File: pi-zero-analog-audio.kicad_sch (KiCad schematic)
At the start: 33 parts, among them J1 GPIO, J2 Screw_Terminal_01x04, J3 Audio Jack, U1 MIC5365-3.3YD5, U2 MC74VHC1GT50, U3 MC74VHC1GT50, U4 PAM8403D

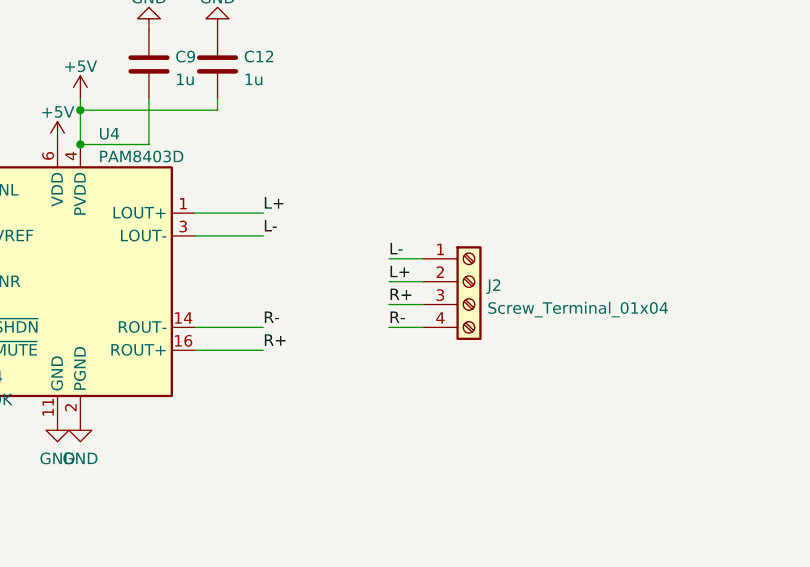
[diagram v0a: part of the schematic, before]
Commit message: Wiring the amplifier on the right side
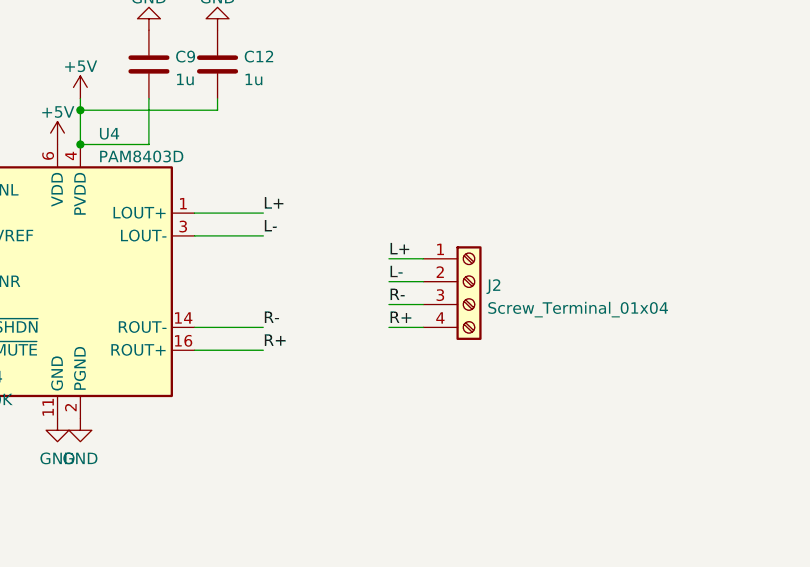
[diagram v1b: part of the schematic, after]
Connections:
- net L+: now also J2.1 (Pin_1); no longer J2.2 (Pin_2)
- net L-: now also J2.2 (Pin_2); no longer J2.1 (Pin_1)
- net R+: now also J2.4 (Pin_4); no longer J2.3 (Pin_3)
- net R-: now also J2.3 (Pin_3); no longer J2.4 (Pin_4)

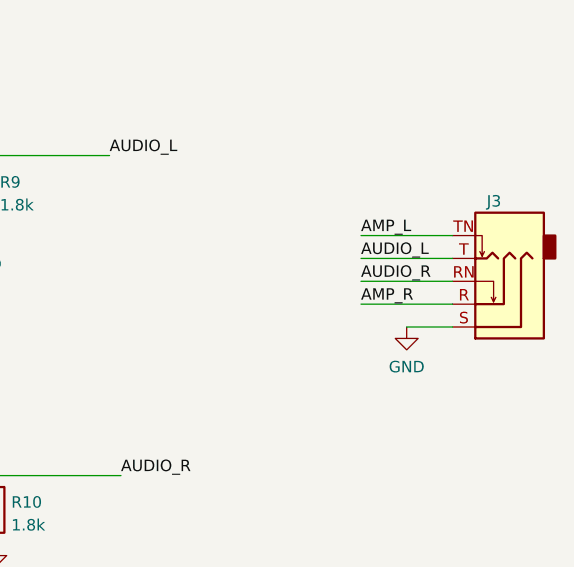
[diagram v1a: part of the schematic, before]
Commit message: Some more efficient design with the same components
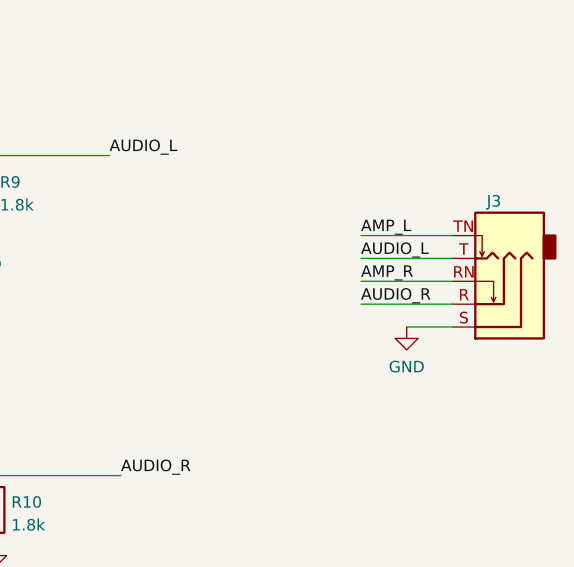
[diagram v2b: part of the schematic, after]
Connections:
- net AMP_R: now also J3.RN; no longer J3.R
- net AUDIO_R: now also J3.R; no longer J3.RN
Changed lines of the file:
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@@
     (stroke (width 0) (type default) (color 0 0 0 0))
+  )
+  (wire (pts (xy 40.64 64.77) (xy 38.1 64.77))
+    (stroke (width 0) (type solid) (color 0 0 0 0))
+  )
+  (wire (pts (xy 162.56 127) (xy 166.37 127))
+    (stroke (width 0) (type default) (color 0 0 0 0))
+  )
+  (wire (pts (xy 76.2 137.16) (xy 85.09 137.16))
+    (stroke (width 0) (type default) (color 0 0 0 0))
+  )
+  (wire (pts (xy 104.14 139.7) (xy 104.14 134.62))
+    (stroke (width 0) (type default) (color 0 0 0 0))
+  )
+  (wire (pts (xy 120.65 33.02) (xy 120.65 22.86))
+    (stroke (width 0) (type default) (color 0 0 0 0))
+  )
+  (wire (pts (xy 146.05 30.48) (xy 152.4 30.48))
+    (stroke (width 0) (type default) (color 0 0 0 0))
+  )
+  (wire (pts (xy 109.22 19.05) (xy 109.22 22.86))
+    (stroke (width 0) (type default) (color 0 0 0 0))
+  )
+  (wire (pts (xy 160.02 30.48) (xy 173.99 30.48))
+    (stroke (width 0) (type default) (color 0 0 0 0))
+  )
+  (wire (pts (xy 40.64 24.13) (xy 40.64 26.67))
+    (stroke (width 0) (type solid) (color 0 0 0 0))
+  )
+  (wire (pts (xy 38.1 62.23) (xy 43.18 62.23))
+    (stroke (width 0) (type default) (color 0 0 0 0))
+  )
+  (wire (pts (xy 201.93 44.45) (xy 212.09 44.45))
+    (stroke (width 0) (type default) (color 0 0 0 0))
+  )
+  (wire (pts (xy 62.23 30.48) (xy 62.23 35.56))
+    (stroke (width 0) (type default) (color 0 0 0 0))
+  )
+  (wire (pts (xy 40.64 39.37) (xy 40.64 46.99))
+    (stroke (width 0) (type solid) (color 0 0 0 0))
+  )
+  (wire (pts (xy 40.64 39.37) (xy 38.1 39.37))
+    (stroke (width 0) (type solid) (color 0 0 0 0))
+  )
+  (wire (pts (xy 104.14 147.32) (xy 104.14 146.05))
+    (stroke (width 0) (type default) (color 0 0 0 0))
+  )
+  (wire (pts (xy 40.64 20.32) (xy 40.64 24.13))
+    (stroke (width 0) (type solid) (color 0 0 0 0))
+  )
+  (wire (pts (xy 140.97 134.62) (xy 148.59 134.62))
+    (stroke (width 0) (type default) (color 0 0 0 0))
+  )
+  (wire (pts (xy 40.64 24.13) (xy 38.1 24.13))
+    (stroke (width 0) (type solid) (color 0 0 0 0))
   )
   (wire (pts (xy 201.93 41.91) (xy 212.09 41.91))
     (stroke (width 0) (type default) (color 0 0 0 0))
   )
-  (wire (pts (xy 40.64 64.77) (xy 38.1 64.77))
-    (stroke (width 0) (type solid) (color 0 0 0 0))
-  )
-  (wire (pts (xy 162.56 127) (xy 166.37 127))
-    (stroke (width 0) (type default) (color 0 0 0 0))
-  )
-  (wire (pts (xy 76.2 137.16) (xy 85.09 137.16))
-    (stroke (width 0) (type default) (color 0 0 0 0))
-  )
-  (wire (pts (xy 104.14 139.7) (xy 104.14 134.62))
-    (stroke (width 0) (type default) (color 0 0 0 0))
-  )
-  (wire (pts (xy 120.65 33.02) (xy 120.65 22.86))
-    (stroke (width 0) (type default) (color 0 0 0 0))
-  )
-  (wire (pts (xy 146.05 30.48) (xy 152.4 30.48))
-    (stroke (width 0) (type default) (color 0 0 0 0))
-  )
-  (wire (pts (xy 109.22 19.05) (xy 109.22 22.86))
-    (stroke (width 0) (type default) (color 0 0 0 0))
-  )
-  (wire (pts (xy 160.02 30.48) (xy 173.99 30.48))
-    (stroke (width 0) (type default) (color 0 0 0 0))
-  )
-  (wire (pts (xy 40.64 24.13) (xy 40.64 26.67))
-    (stroke (width 0) (type solid) (color 0 0 0 0))
-  )
-  (wire (pts (xy 38.1 62.23) (xy 43.18 62.23))
-    (stroke (width 0) (type default) (color 0 0 0 0))
-  )
-  (wire (pts (xy 201.93 44.45) (xy 212.09 44.45))
-    (stroke (width 0) (type default) (color 0 0 0 0))
-  )
-  (wire (pts (xy 62.23 30.48) (xy 62.23 35.56))
-    (stroke (width 0) (type default) (color 0 0 0 0))
-  )
-  (wire (pts (xy 40.64 39.37) (xy 40.64 46.99))
-    (stroke (width 0) (type solid) (color 0 0 0 0))
-  )
-  (wire (pts (xy 40.64 39.37) (xy 38.1 39.37))
-    (stroke (width 0) (type solid) (color 0 0 0 0))
-  )
-  (wire (pts (xy 104.14 147.32) (xy 104.14 146.05))
-    (stroke (width 0) (type default) (color 0 0 0 0))
-  )
-  (wire (pts (xy 40.64 20.32) (xy 40.64 24.13))
-    (stroke (width 0) (type solid) (color 0 0 0 0))
-  )
-  (wire (pts (xy 140.97 134.62) (xy 148.59 134.62))
-    (stroke (width 0) (type default) (color 0 0 0 0))
-  )
-  (wire (pts (xy 40.64 24.13) (xy 38.1 24.13))
-    (stroke (width 0) (type solid) (color 0 0 0 0))
-  )
   (wire (pts (xy 120.65 22.86) (xy 109.22 22.86))
     (stroke (width 0) (type default) (color 0 0 0 0))
@@
     (effects (font (size 1.27 1.27)) (justify left bottom))
   )
-  (label "AUDIO_R" (at 201.93 44.45 0)
-    (effects (font (size 1.27 1.27)) (justify left bottom))
-  )
   (label "AMP_L" (at 76.2 119.38 0)
     (effects (font (size 1.27 1.27)) (justify left bottom))
   )
+  (label "AUDIO_R" (at 201.93 46.99 0)
+    (effects (font (size 1.27 1.27)) (justify left bottom))
+  )
   (label "MUTE" (at 76.2 137.16 0)
     (effects (font (size 1.27 1.27)) (justify left bottom))
@@
     (effects (font (size 1.27 1.27)) (justify left bottom))
   )
-  (label "AMP_R" (at 201.93 46.99 0)
-    (effects (font (size 1.27 1.27)) (justify left bottom))
-  )
   (label "MUTE" (at 43.18 67.31 0)
     (effects (font (size 1.27 1.27)) (justify left bottom))
@@
     (effects (font (size 1.27 1.27)) (justify left bottom))
   )
+  (label "AMP_R" (at 201.93 44.45 0)
+    (effects (font (size 1.27 1.27)) (justify left bottom))
+  )

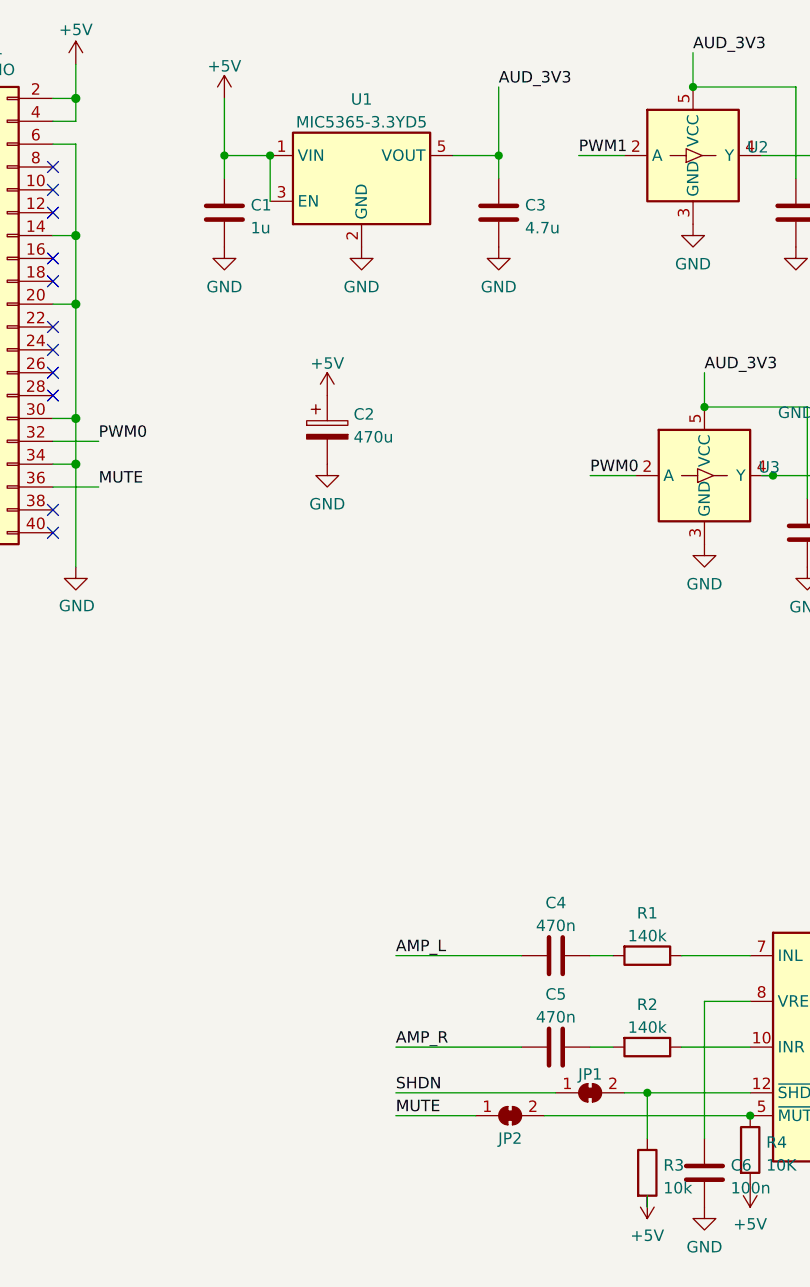
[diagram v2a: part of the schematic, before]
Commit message: Allow alternate LDO with Band-Gap Bypass
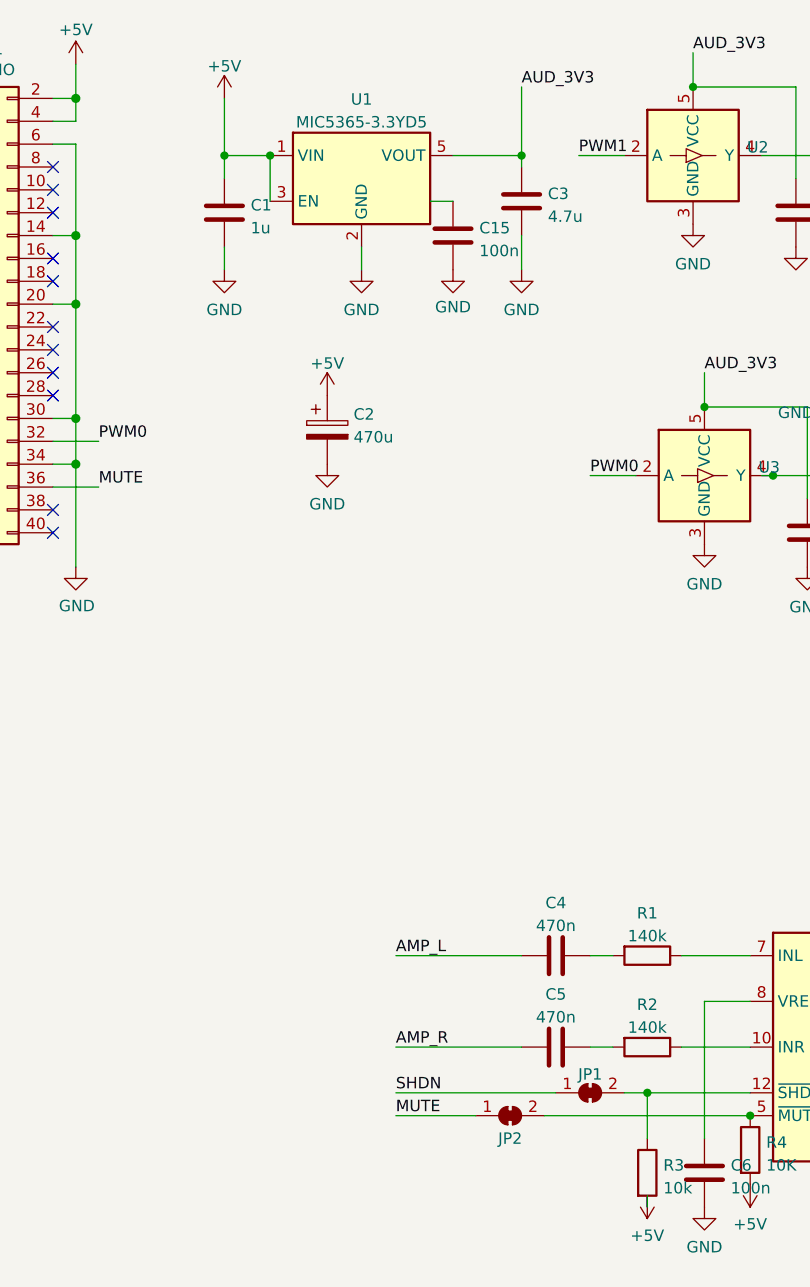
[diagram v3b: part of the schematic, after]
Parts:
- added C15: 100n, Capacitor_SMD:C_0805_2012Metric_Pad1.18x1.45mm_HandSolder, symbol Device:C
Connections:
- net GND: now also C15.2
- net at U1.4 (NC): now also C15.1
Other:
- moved on the sheet: C3

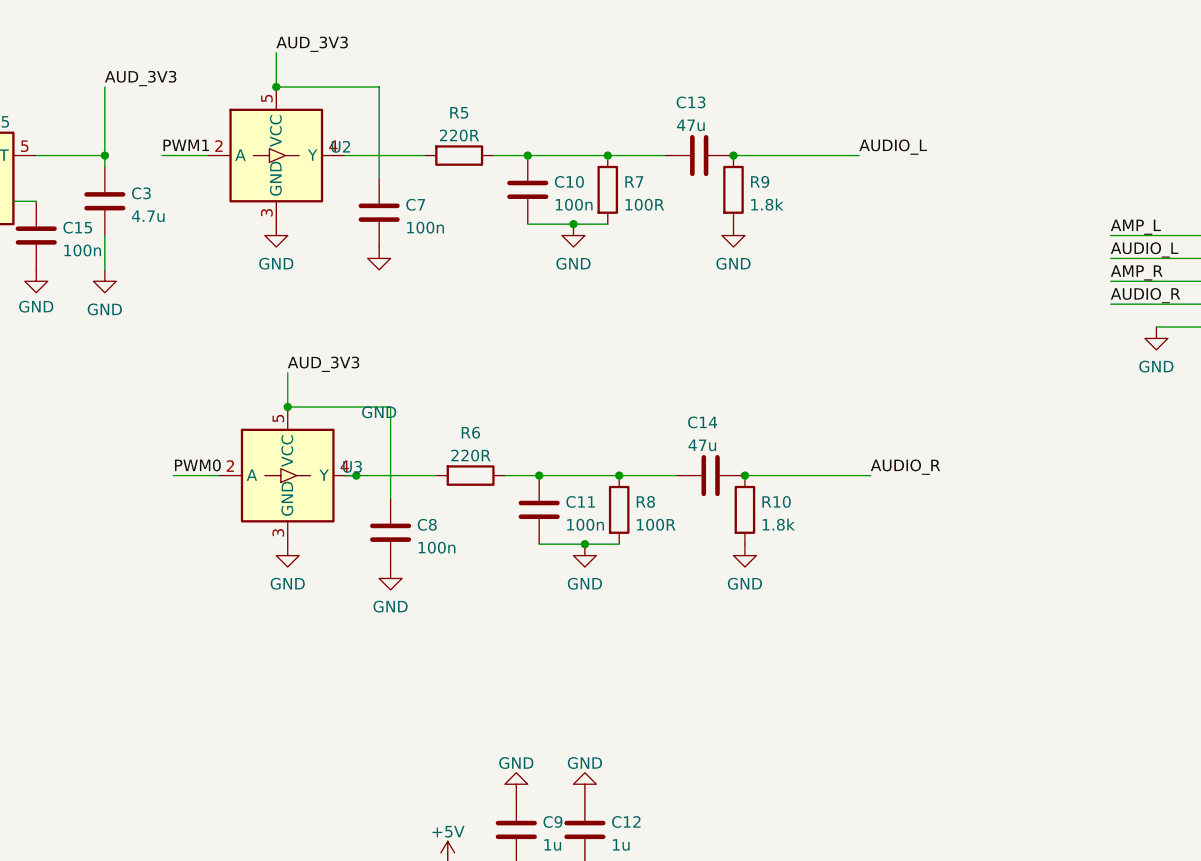
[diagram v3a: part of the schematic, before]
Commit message: Adding ferrite beads on 3V3 rails
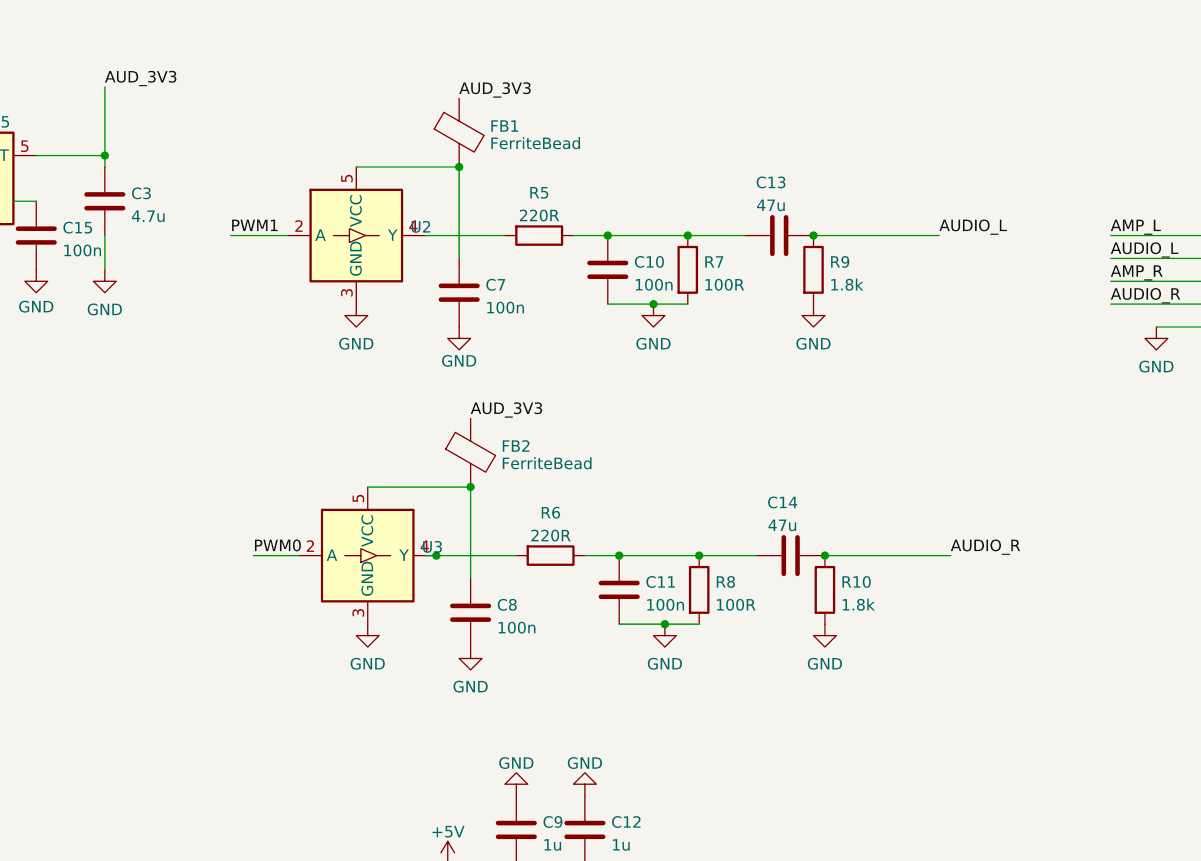
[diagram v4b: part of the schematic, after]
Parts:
- added FB1, FB2: FerriteBead, PCM_Ferrite_SMD_Handsoldering_AKL:Ferrite_0805_2012Metric_Pad1.15x1.40mm_BigPads, symbol Device:FerriteBead
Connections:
- net AUD_3V3: now also FB1.1, FB2.1; no longer C7.1, C8.1, U2.5 (VCC), U3.5 (VCC)
- new net: C8.1, FB2.2, U3.5 (VCC)
- new net: C7.1, FB1.2, U2.5 (VCC)
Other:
- moved on the sheet: C10, C11, C13, C14, C7, C8, R10, R5, R6, R7, R8, R9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
